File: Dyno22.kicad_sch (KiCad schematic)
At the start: 49 parts, among them J1 Pwr Input, J2 Display, J3 Pwr Output, J4 BPM & Sensors, J7 UART, SW1 SW_DPST_x2, U1 TS2937CW50, U2 LM324, U3 Demux

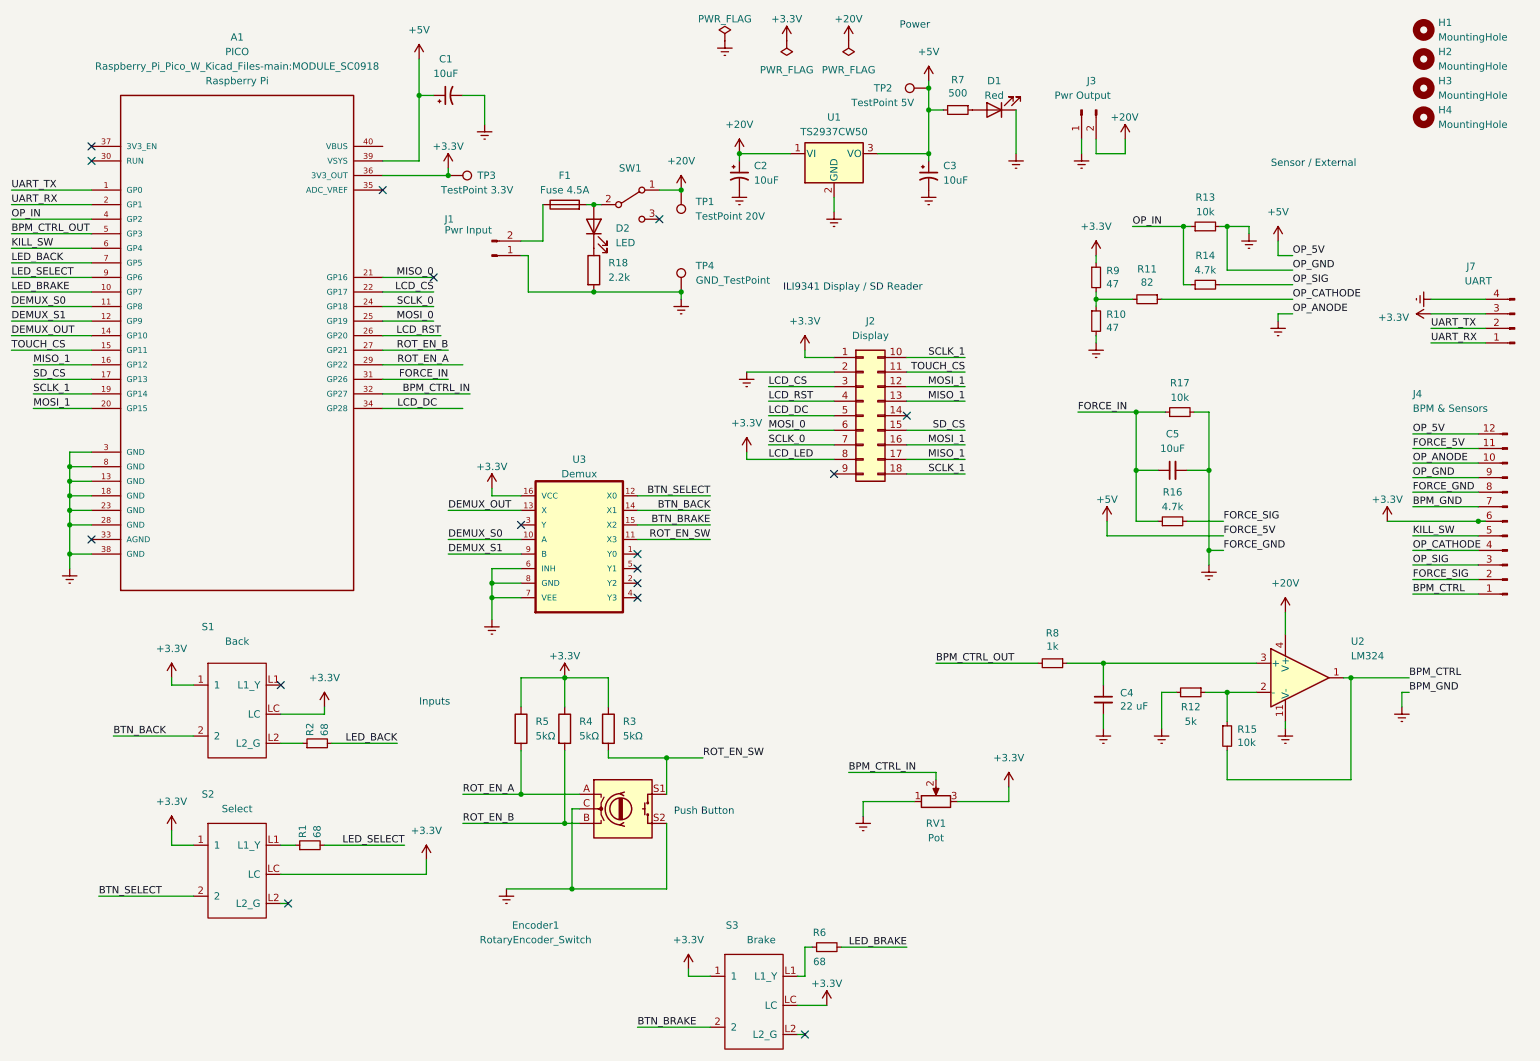
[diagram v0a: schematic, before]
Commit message: made some passive components 0805 and changed some routing
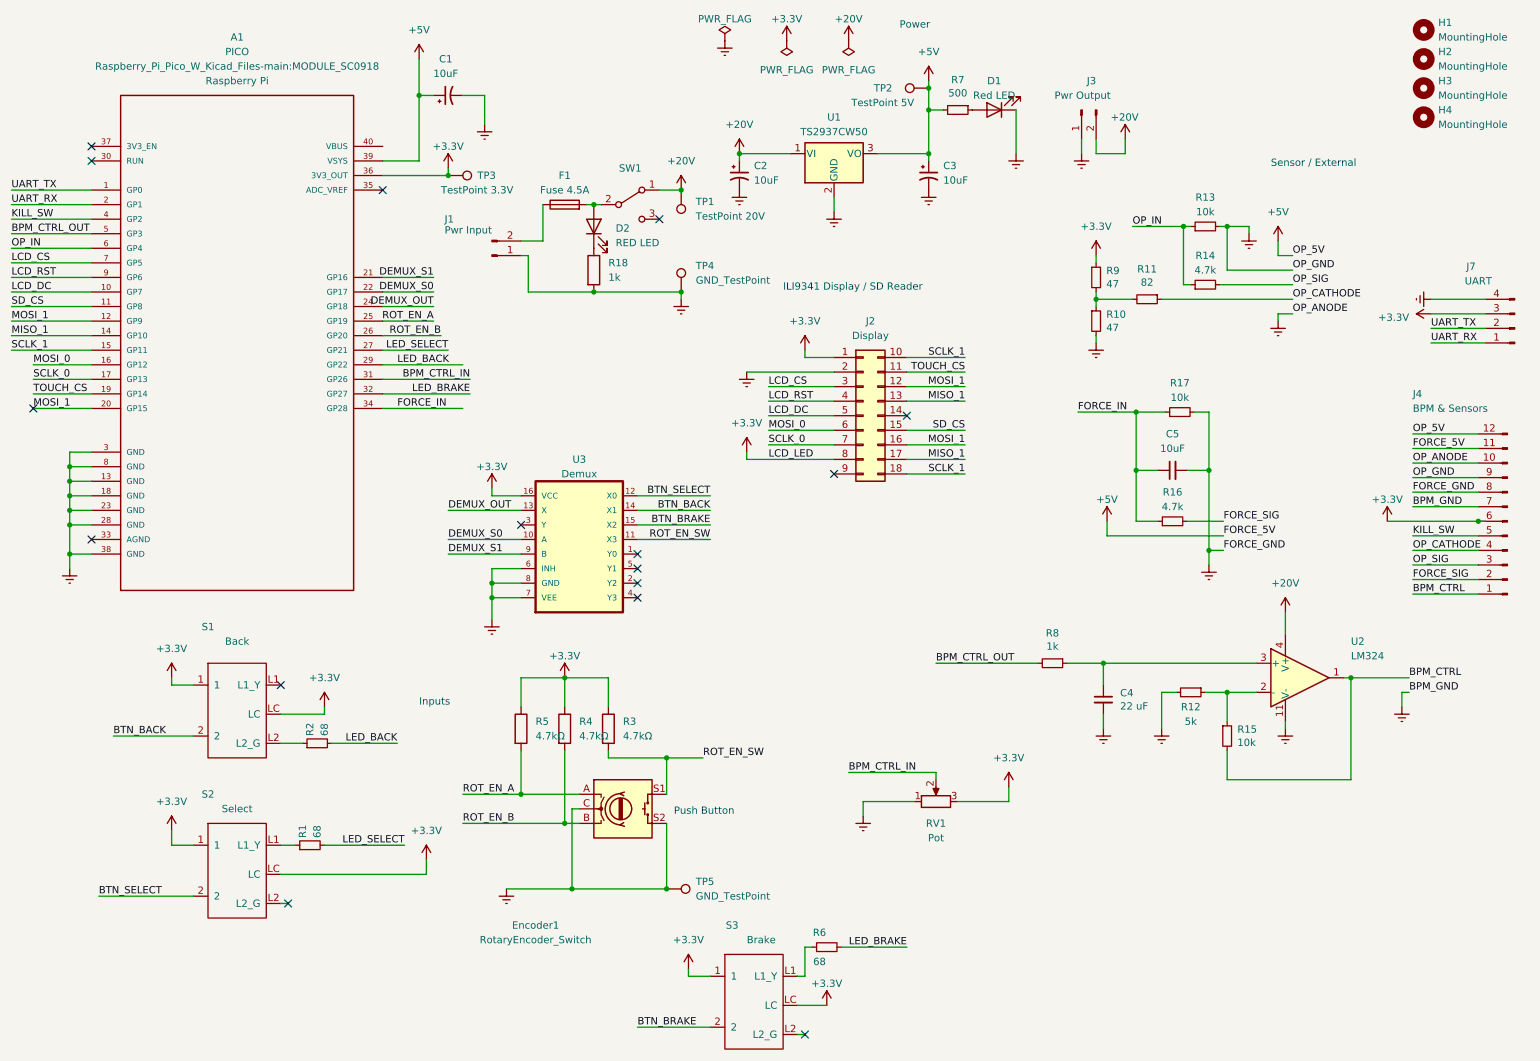
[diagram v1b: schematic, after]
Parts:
- added TP5: GND_TestPoint, TestPoint:TestPoint_Loop_D2.60mm_Drill1.4mm_Beaded, symbol Connector:TestPoint
- D1: value Red -> Red LED
- D2: value LED -> RED LED; footprint LED_SMD:LED_0603_1608Metric -> LED_SMD:LED_0805_2012Metric
- Encoder1: footprint Rotary_Encoder:RotaryEncoder_Alps_EC11E_Vertical_H20mm -> Rotary_Encoder:RotaryEncoder_Alps_EC12E-Switch_Vertical_H20mm_CircularMountingHoles
- R18: value 2.2k -> 1k; footprint Resistor_SMD:R_0402_1005Metric -> Resistor_SMD:R_0805_2012Metric
- R3, R4, R5: value 5kΩ -> 4.7kΩ
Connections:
- net MISO_0 is gone; now on net DEMUX_S1: A1.21 (GP16)
- net BPM_CTRL_IN: now also A1.31 (GP26); no longer A1.32 (GP27)
- net DEMUX_OUT: now also A1.24 (GP18); no longer A1.14 (GP10)
- net DEMUX_S0: now also A1.22 (GP17); no longer A1.11 (GP8)
- net DEMUX_S1: no longer A1.12 (GP9)
- net Earth: now also TP5.1
- net FORCE_IN: now also A1.34 (GP28); no longer A1.31 (GP26)
- net KILL_SW: now also A1.4 (GP2); no longer A1.6 (GP4)
- net LCD_CS: now also A1.7 (GP5); no longer A1.22 (GP17)
- net LCD_DC: now also A1.10 (GP7); no longer A1.34 (GP28)
- net LCD_RST: now also A1.9 (GP6); no longer A1.26 (GP20)
- net LED_BACK: now also A1.29 (GP22); no longer A1.7 (GP5)
- net LED_BRAKE: now also A1.32 (GP27); no longer A1.10 (GP7)
- net LED_SELECT: now also A1.27 (GP21); no longer A1.9 (GP6)
- net MISO_1: now also A1.14 (GP10); no longer A1.16 (GP12)
- net MOSI_0: now also A1.16 (GP12); no longer A1.25 (GP19)
- net MOSI_1: now also A1.12 (GP9)
- net OP_IN: now also A1.6 (GP4); no longer A1.4 (GP2)
- net ROT_EN_A: now also A1.25 (GP19); no longer A1.29 (GP22)
- net ROT_EN_B: now also A1.26 (GP20); no longer A1.27 (GP21)
- net SCLK_0: now also A1.17 (GP13); no longer A1.24 (GP18)
- net SCLK_1: now also A1.15 (GP11); no longer A1.19 (GP14)
- net SD_CS: now also A1.11 (GP8); no longer A1.17 (GP13)
- net TOUCH_CS: now also A1.19 (GP14); no longer A1.15 (GP11)
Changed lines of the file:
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@@
   (junction (at 100.33 116.84) (diameter 0) (color 0 0 0 0)
   )
+  (junction (at 130.81 167.64) (diameter 0) (color 0 0 0 0)
+  )
   (junction (at 26.67 93.98) (diameter 0) (color 0 0 0 0)
   )
@@
   (no_connect (at 129.54 50.8))
   (no_connect (at 63.5 132.08))
+  (no_connect (at 20.32 83.82))
   (no_connect (at 105.41 104.14))
   (no_connect (at 154.94 193.04))
@@
   (no_connect (at 125.73 116.84))
   (no_connect (at 81.28 45.72))
-  (no_connect (at 90.17 60.96))
   (no_connect (at 64.77 170.18))
   (no_connect (at 125.73 111.76))
@@
     (stroke (width 0) (type default))
   )
-  (wire (pts (xy 81.28 78.74) (xy 92.71 78.74))
+  (wire (pts (xy 81.28 78.74) (xy 96.52 78.74))
     (stroke (width 0) (type default))
   )
@@
     (effects (font (size 1.27 1.27)) (justify right bottom))
   )
-  (label "DEMUX_S1" (at 16.51 68.58 0) (fields_autoplaced)
+  (label "MOSI_1" (at 16.51 68.58 0) (fields_autoplaced)
     (effects (font (size 1.27 1.27)) (justify left bottom))
   )
@@
     (effects (font (size 1.27 1.27)) (justify left bottom))
   )
-  (label "SCLK_1" (at 20.32 81.28 0) (fields_autoplaced)
+  (label "TOUCH_CS" (at 20.32 81.28 0) (fields_autoplaced)
     (effects (font (size 1.27 1.27)) (justify left bottom))
   )
@@
     (effects (font (size 1.27 1.27)) (justify left bottom))
   )
-  (label "DEMUX_S0" (at 16.51 66.04 0) (fields_autoplaced)
+  (label "SD_CS" (at 16.51 66.04 0) (fields_autoplaced)
     (effects (font (size 1.27 1.27)) (justify left bottom))
   )
@@
     (effects (font (size 1.27 1.27)) (justify left bottom))
   )
-  (label "LCD_CS" (at 90.17 63.5 180) (fields_autoplaced)
+  (label "DEMUX_S0" (at 90.17 63.5 180) (fields_autoplaced)
     (effects (font (size 1.27 1.27)) (justify right bottom))
   )
@@
     (effects (font (size 1.27 1.27)) (justify left bottom))
   )
-  (label "LCD_RST" (at 91.44 71.12 180) (fields_autoplaced)
+  (label "ROT_EN_B" (at 91.44 71.12 180) (fields_autoplaced)
     (effects (font (size 1.27 1.27)) (justify right bottom))
   )
-  (label "KILL_SW" (at 16.51 55.88 0) (fields_autoplaced)
+  (label "OP_IN" (at 16.51 55.88 0) (fields_autoplaced)
     (effects (font (size 1.27 1.27)) (justify left bottom))
   )
@@
     (effects (font (size 1.27 1.27)) (justify left bottom))
   )
-  (label "MISO_0" (at 90.17 60.96 180) (fields_autoplaced)
+  (label "DEMUX_S1" (at 90.17 60.96 180) (fields_autoplaced)
     (effects (font (size 1.27 1.27)) (justify right bottom))
   )
-  (label "DEMUX_OUT" (at 16.51 71.12 0) (fields_autoplaced)
+  (label "MISO_1" (at 16.51 71.12 0) (fields_autoplaced)
     (effects (font (size 1.27 1.27)) (justify left bottom))
   )
@@
     (effects (font (size 1.27 1.27)) (justify right bottom))
   )
-  (label "LED_BRAKE" (at 16.51 63.5 0) (fields_autoplaced)
+  (label "LCD_DC" (at 16.51 63.5 0) (fields_autoplaced)
     (effects (font (size 1.27 1.27)) (justify left bottom))
   )
-  (label "LCD_DC" (at 83.82 83.82 0) (fields_autoplaced)
+  (label "FORCE_IN" (at 83.82 83.82 0) (fields_autoplaced)
     (effects (font (size 1.27 1.27)) (justify left bottom))
   )
@@
     (effects (font (size 1.27 1.27)) (justify left bottom))
   )
-  (label "MISO_1" (at 20.32 76.2 0) (fields_autoplaced)
+  (label "MOSI_0" (at 20.32 76.2 0) (fields_autoplaced)
     (effects (font (size 1.27 1.27)) (justify left bottom))
   )
@@
     (effects (font (size 1.27 1.27)) (justify left bottom))
   )
-  (label "ROT_EN_B" (at 92.71 73.66 180) (fields_autoplaced)
+  (label "LED_SELECT" (at 92.71 73.66 180) (fields_autoplaced)
     (effects (font (size 1.27 1.27)) (justify right bottom))
   )
-  (label "ROT_EN_A" (at 83.82 76.2 0) (fields_autoplaced)
+  (label "LED_BACK" (at 83.82 76.2 0) (fields_autoplaced)
     (effects (font (size 1.27 1.27)) (justify left bottom))
   )
-  (label "LED_SELECT" (at 16.51 60.96 0) (fields_autoplaced)
+  (label "LCD_RST" (at 16.51 60.96 0) (fields_autoplaced)
     (effects (font (size 1.27 1.27)) (justify left bottom))
   )
@@
     (effects (font (size 1.27 1.27)) (justify left bottom))
   )
-  (label "SCLK_0" (at 90.17 66.04 180) (fields_autoplaced)
+  (label "DEMUX_OUT" (at 90.17 66.04 180) (fields_autoplaced)
     (effects (font (size 1.27 1.27)) (justify right bottom))
   )
@@
     (effects (font (size 1.27 1.27)) (justify left bottom))
   )
-  (label "OP_IN" (at 16.51 50.8 0) (fields_autoplaced)
+  (label "KILL_SW" (at 16.51 50.8 0) (fields_autoplaced)
     (effects (font (size 1.27 1.27)) (justify left bottom))
   )
@@
     (effects (font (size 1.27 1.27)) (justify right bottom))
   )
-  (label "TOUCH_CS" (at 16.51 73.66 0) (fields_autoplaced)
+  (label "SCLK_1" (at 16.51 73.66 0) (fields_autoplaced)
     (effects (font (size 1.27 1.27)) (justify left bottom))
   )
@@
     (effects (font (size 1.27 1.27)) (justify right bottom))
   )
-  (label "FORCE_IN" (at 92.71 78.74 180) (fields_autoplaced)
+  (label "BPM_CTRL_IN" (at 96.52 78.74 180) (fields_autoplaced)
     (effects (font (size 1.27 1.27)) (justify right bottom))
   )
@@
     (effects (font (size 1.27 1.27)) (justify left bottom))
   )
-  (label "BPM_CTRL_IN" (at 96.52 81.28 180) (fields_autoplaced)
+  (label "LED_BRAKE" (at 96.52 81.28 180) (fields_autoplaced)
     (effects (font (size 1.27 1.27)) (justify right bottom))
   )
@@
     (effects (font (size 1.27 1.27)) (justify right bottom))
   )
-  (label "MOSI_0" (at 90.17 68.58 180) (fields_autoplaced)
+  (label "ROT_EN_A" (at 90.17 68.58 180) (fields_autoplaced)
     (effects (font (size 1.27 1.27)) (justify right bottom))
   )
-  (label "LED_BACK" (at 16.51 58.42 0) (fields_autoplaced)
+  (label "LCD_CS" (at 16.51 58.42 0) (fields_autoplaced)
     (effects (font (size 1.27 1.27)) (justify left bottom))
   )
-  (label "SD_CS" (at 20.32 78.74 0) (fields_autoplaced)
+  (label "SCLK_0" (at 20.32 78.74 0) (fields_autoplaced)
     (effects (font (size 1.27 1.27)) (justify left bottom))
   )
@@
       (effects (font (size 1.27 1.27)) (justify left))
     )
-    (property "Value" "5kΩ" (at 107.95 140.97 0)
+    (property "Value" "4.7kΩ" (at 107.95 140.97 0)
       (effects (font (size 1.27 1.27)) (justify left))
     )
@@
     )
   )
+  (symbol (lib_id "Connector:TestPoint") (at 130.81 167.64 270) (unit 1)
+    (in_bom yes) (on_board yes) (dnp no) (fields_autoplaced)
+    (property "Reference" "TP5" (at 135.89 166.37 90)
+      (effects (font (size 1.27 1.27)) (justify left))
+    )
+    (property "Value" "GND_TestPoint" (at 135.89 168.91 90)
+      (effects (font (size 1.27 1.27)) (justify left))
+    )
+    (property "Footprint" "TestPoint:TestPoint_Loop_D2.60mm_Drill1.4mm_Beaded" (at 130.81 172.72 0)
+      (effects (font (size 1.27 1.27)) hide)
+    )
+    (property "Datasheet" "~" (at 130.81 172.72 0)
+      (effects (font (size 1.27 1.27)) hide)
+    )
+    (pin "1")
+    (instances
+      (project "Dyno22"
+        (path "/7271225a-6695-4332-8687-d26f1f45d708"
+          (reference "TP5") (unit 1)
+        )
+      )
+    )
+  )
   (symbol (lib_id "power:+3.3V") (at 205.74 57.15 0) (unit 1)
     (in_bom yes) (on_board yes) (dnp no) (fields_autoplaced)
@@
       (effects (font (size 1.27 1.27)) (justify left))
     )
-    (property "Value" "5kΩ" (at 123.19 140.97 0)
+    (property "Value" "4.7kΩ" (at 123.19 140.97 0)
       (effects (font (size 1.27 1.27)) (justify left))
     )
@@
       (effects (font (size 1.27 1.27)) (justify right))
     )
-    (property "Value" "LED" (at 121.92 54.9275 90)
+    (property "Value" "RED LED" (at 121.92 54.9275 90)
       (effects (font (size 1.27 1.27)) (justify right))
     )
-    (property "Footprint" "LED_SMD:LED_0603_1608Metric" (at 118.11 52.07 0)
+    (property "Footprint" "LED_SMD:LED_0805_2012Metric" (at 118.11 52.07 0)
       (effects (font (size 1.27 1.27)) hide)
     )
@@
       (effects (font (size 1.27 1.27)))
     )
-    (property "Value" "Red" (at 187.96 29.21 0)
+    (property "Value" "Red LED" (at 187.96 29.21 0)
       (effects (font (size 1.27 1.27)))
     )
@@
       (effects (font (size 1.27 1.27)) (justify left))
     )
-    (property "Value" "5kΩ" (at 115.57 140.97 0)
+    (property "Value" "4.7kΩ" (at 115.57 140.97 0)
       (effects (font (size 1.27 1.27)) (justify left))
     )
@@
       (effects (font (size 1.27 1.27)))
     )
-    (property "Footprint" "Rotary_Encoder:RotaryEncoder_Alps_EC11E_Vertical_H20mm" (at 119.38 149.606 0)
+    (property "Footprint" "Rotary_Encoder:RotaryEncoder_Alps_EC12E-Switch_Vertical_H20mm_CircularMountingHoles" (at 119.38 149.606 0)
       (effects (font (size 1.27 1.27)) hide)
     )
@@
       (effects (font (size 1.27 1.27)) (justify left))
     )
-    (property "Value" "2.2k" (at 120.65 60.96 0)
+    (property "Value" "1k" (at 120.65 60.96 0)
       (effects (font (size 1.27 1.27)) (justify left))
     )
-    (property "Footprint" "Resistor_SMD:R_0402_1005Metric" (at 116.332 59.69 90)
+    (property "Footprint" "Resistor_SMD:R_0805_2012Metric" (at 116.332 59.69 90)
       (effects (font (size 1.27 1.27)) hide)
     )

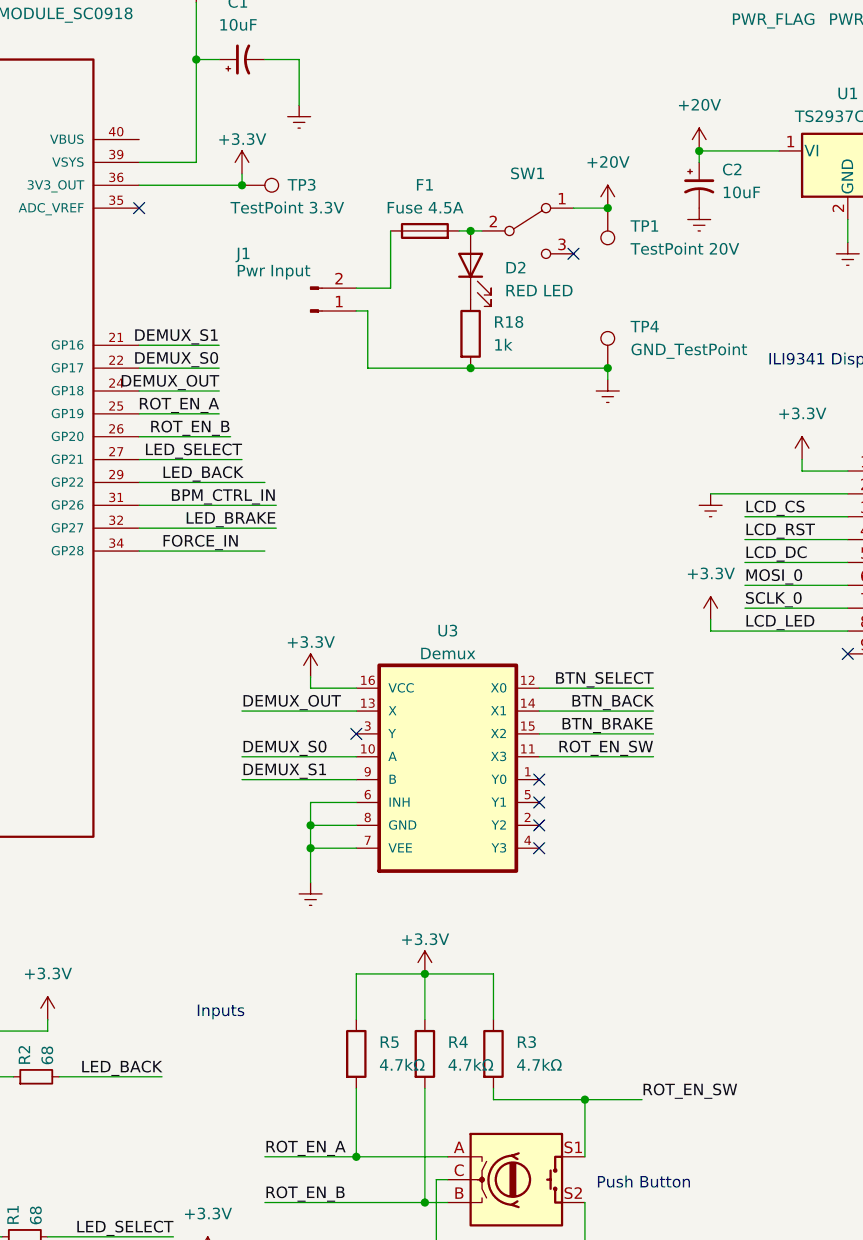
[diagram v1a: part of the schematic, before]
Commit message: Added demux changed LED location changed some Rs
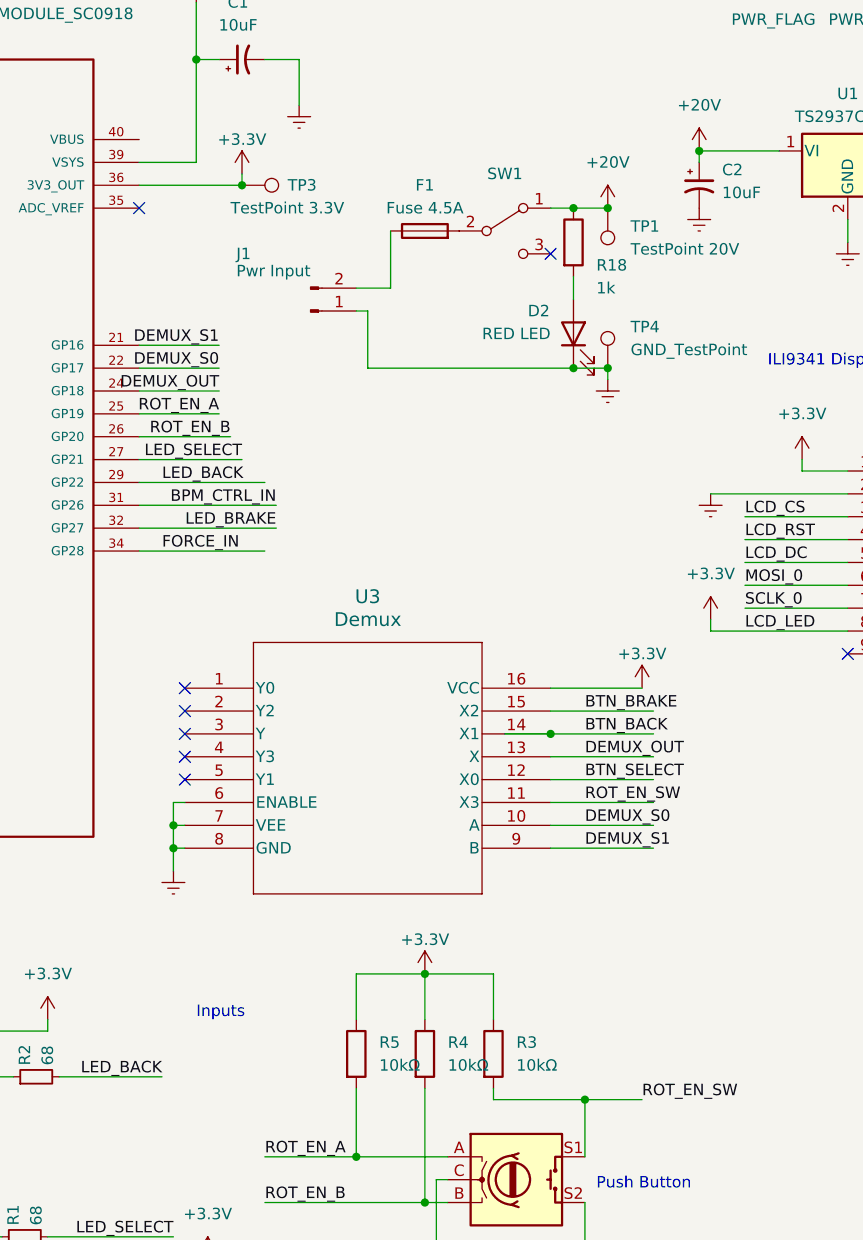
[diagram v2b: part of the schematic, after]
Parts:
- removed U3: Demux, 74HC4052PW-footprints_LOCAL:TSSOP16_5P1X4P5_NEX, symbol 74HC4052:74HC4052
- added U3: Demux, SOIC-16WB_ONS, symbol 2024-01-20_19-44-30:MC74HC4052ADWR2G
- R3, R4, R5: value 4.7kΩ -> 10kΩ
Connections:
- net +24V: now also R18.1
- net +3.3V: now also U3.16 (VCC)
- net BTN_BACK: now also U3.14 (X1)
- net BTN_BRAKE: now also U3.15 (X2)
- net BTN_SELECT: now also U3.12 (X0)
- net DEMUX_OUT: now also U3.13 (X)
- net DEMUX_S0: now also U3.10 (A)
- net DEMUX_S1: now also U3.9 (B)
- net Earth: now also D2.1 (K), U3.6 (ENABLE), U3.7 (VEE), U3.8 (GND); no longer R18.2
- net ROT_EN_SW: now also U3.11 (X3)
- net at F1.2, SW1.2 (B): no longer D2.2 (A)
- new net: D2.2 (A), R18.2
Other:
- moved on the sheet: D2, R18, SW1
